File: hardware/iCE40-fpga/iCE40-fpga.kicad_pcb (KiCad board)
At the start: 4 copper layers, 50 x 22.9 mm, 69 parts, among them J1 USB_B_Micro, J2 JST_PH, J3 Feather, Q1 DMP2045U, U1 MCP73831-2-OT, U2 W25Q32JVZP, U3 AP2112K-3.3, U4 ICE40UP5K-SG48ITR, U5 NCV8114ASN120T1G, U6 93C46B, U7 FT2232H, X1 DSC6101CI1A

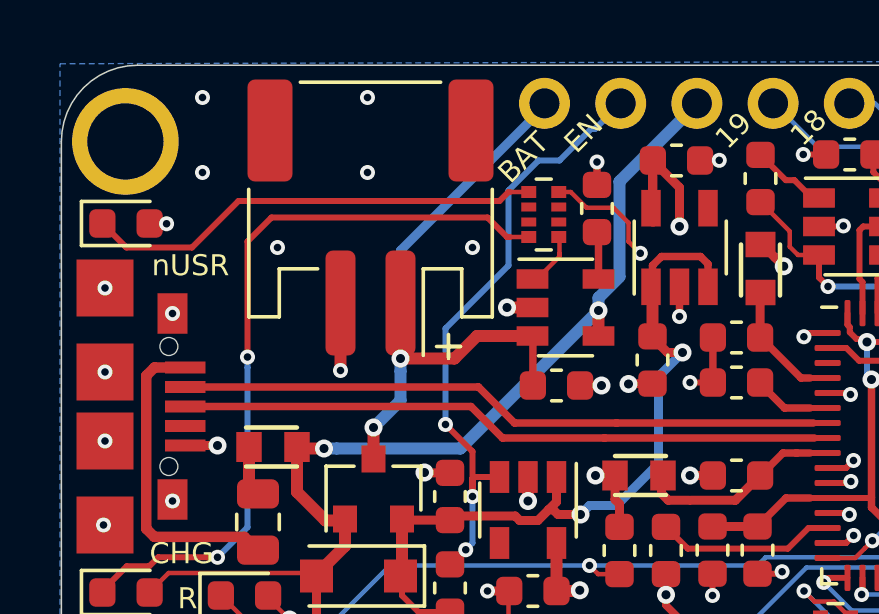
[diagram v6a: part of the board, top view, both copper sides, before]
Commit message: moved battery connector and generated new gerbers for FPGA
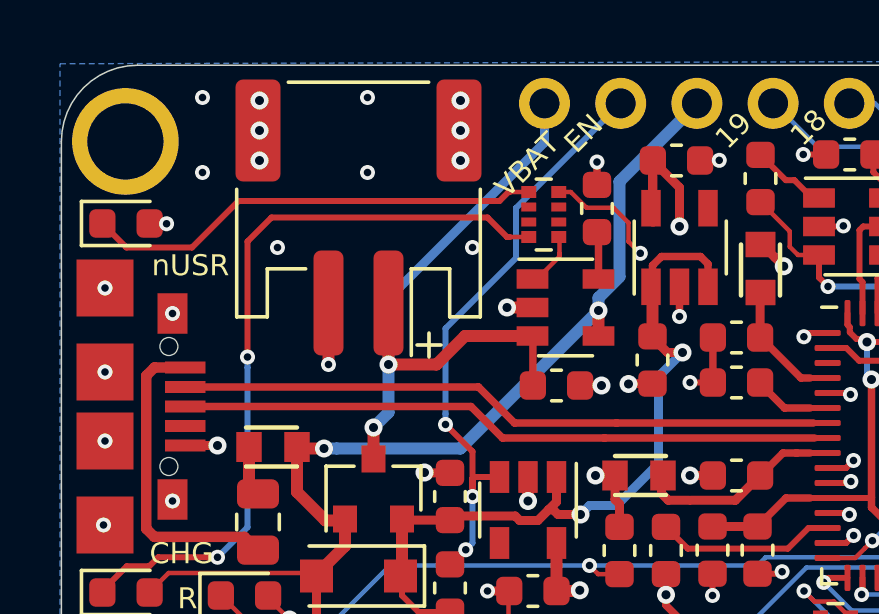
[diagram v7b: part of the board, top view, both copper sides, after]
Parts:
- moved J2 0.40 mm to (36.2, 27.5)
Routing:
- net GND: track 46.5 -> 44.5 mm
- net (no net): vias 0 -> 6
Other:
- board text added: "VBAT"
- board text removed: "BAT"
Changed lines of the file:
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@@
   (general
     (thickness 1.6)
-    (drawings 59)
+    (drawings 58)
     (tracks 1362)
     (zones 0)
@@
   )
   (module josh-connectors:JST_PH_S2B-PH-SM4-TB_1x02-1MP_P2.00mm_Horizontal (layer F.Cu)
-    (at 36.6 27.5 180)
+    (at 36.2 27.5 180)
     (descr "JST PH series connector, S2B-PH-SM4-TB (http://www.jst-mfg.com/product/pdf/eng/ePH.pdf), generated with kicad-footprint-generator")
     (tags "connector JST PH top entry")
@@
       (effects (font (size 1 1) (thickness 0.15)) (justify mirror))
     )
-    (fp_text value 21 (at -2.475 -0.025) (layer B.SilkS)
+    (fp_text value 21 (at -2.4 -0.025) (layer B.SilkS)
       (effects (font (size 1 1) (thickness 0.15)) (justify mirror))
     )
@@
       (effects (font (size 1 1) (thickness 0.15)) (justify mirror))
     )
-    (fp_text value 23 (at -2.5 0) (layer B.SilkS)
+    (fp_text value 23 (at -2.4 0) (layer B.SilkS)
       (effects (font (size 1 1) (thickness 0.15)) (justify mirror))
     )
@@
       (effects (font (size 1 1) (thickness 0.15)) (justify mirror))
     )
-    (fp_text value 20 (at 2.525 0) (layer B.SilkS)
+    (fp_text value 20 (at 2.35 0) (layer B.SilkS)
       (effects (font (size 1 1) (thickness 0.15)) (justify mirror))
     )
@@
       (effects (font (size 1 1) (thickness 0.15)) (justify mirror))
     )
-    (fp_text value 22 (at 2.5 0) (layer B.SilkS)
+    (fp_text value 22 (at 2.35 0) (layer B.SilkS)
       (effects (font (size 1 1) (thickness 0.15)) (justify mirror))
     )
@@
     )
   )
-  (gr_line (start 39.6 31.8) (end 38.8 31.8) (layer F.SilkS) (width 0.12))
-  (gr_line (start 39.2 31.8) (end 39.6 31.8) (layer F.SilkS) (width 0.12))
-  (gr_line (start 39.2 31.4) (end 39.2 32.2) (layer F.SilkS) (width 0.12))
+  (gr_line (start 38.95 31.75) (end 38.15 31.75) (layer F.SilkS) (width 0.12))
+  (gr_line (start 38.55 31.35) (end 38.55 32.15) (layer F.SilkS) (width 0.12))
   (gr_text 14 (at 62.7 25.575) (layer B.SilkS)
     (effects (font (size 1 1) (thickness 0.15)) (justify mirror))
@@
     (effects (font (size 1 1) (thickness 0.15)) (justify mirror))
   )
-  (gr_text BAT (at 42.375 25.575) (layer B.SilkS)
+  (gr_text VBAT (at 41.95 25.6) (layer B.SilkS)
     (effects (font (size 1 1) (thickness 0.15)) (justify mirror))
   )
@@
     (effects (font (size 0.7 0.7) (thickness 0.125)))
   )
-  (gr_text BAT (at 41.7 25.5 45) (layer F.SilkS)
+  (gr_text VBAT (at 41.825 25.75 45) (layer F.SilkS)
     (effects (font (size 0.7 0.7) (thickness 0.125)))
   )
@@
     (effects (font (size 0.7 0.7) (thickness 0.15)))
   )
+  (via (at 32.9 25.6) (size 0.6) (drill 0.3) (layers F.Cu B.Cu) (net 0))
+  (via (at 32.9 24.6) (size 0.6) (drill 0.3) (layers F.Cu B.Cu) (net 0))
+  (via (at 32.9 23.6) (size 0.6) (drill 0.3) (layers F.Cu B.Cu) (net 0))
+  (via (at 39.6 23.6) (size 0.6) (drill 0.3) (layers F.Cu B.Cu) (net 0))
+  (via (at 39.6 25.6) (size 0.6) (drill 0.3) (layers F.Cu B.Cu) (net 0))
+  (via (at 39.6 24.6) (size 0.6) (drill 0.3) (layers F.Cu B.Cu) (net 0))
   (segment (start 39.25 37.5875) (end 37.6875 37.5875) (width 0.3) (layer F.Cu) (net 1))
   (segment (start 37.6875 37.5875) (end 37.65 37.55) (width 0.3) (layer F.Cu) (net 1))
@@
   (segment (start 42.0125 31.4625) (end 42 31.45) (width 0.25) (layer F.Cu) (net 2))
   (segment (start 42.35 23.65) (end 42.4 23.7) (width 0.3) (layer B.Cu) (net 2))
-  (segment (start 37.6 30.35) (end 37.6 29.6) (width 0.4) (layer F.Cu) (net 2))
-  (segment (start 37.6 33.6) (end 37.6 32.624276) (width 0.4) (layer B.Cu) (net 2))
-  (segment (start 37.6 32.624276) (end 37.6 32.200012) (width 0.4) (layer B.Cu) (net 2))
-  (segment (start 37.6 28.6) (end 37.6 31.775748) (width 0.3) (layer B.Cu) (net 2))
-  (via (at 37.6 32.200012) (size 0.6) (drill 0.3) (layers F.Cu B.Cu) (net 2))
-  (segment (start 37.6 31.775748) (end 37.6 32.200012) (width 0.3) (layer B.Cu) (net 2))
-  (segment (start 42.4 23.8) (end 37.6 28.6) (width 0.3) (layer B.Cu) (net 2))
-  (segment (start 36.7 34.5) (end 37.6 33.6) (width 0.4) (layer B.Cu) (net 2))
-  (segment (start 37.6 30.8) (end 37.6 32.200012) (width 0.4) (layer F.Cu) (net 2))
-  (segment (start 37.600012 32.2) (end 37.6 32.200012) (width 0.4) (layer F.Cu) (net 2))
-  (segment (start 39.4 32.2) (end 37.600012 32.2) (width 0.4) (layer F.Cu) (net 2))
-  (segment (start 42 31.45) (end 40.15 31.45) (width 0.4) (layer F.Cu) (net 2))
-  (segment (start 40.15 31.45) (end 39.4 32.2) (width 0.4) (layer F.Cu) (net 2))
+  (segment (start 36.7 34.5) (end 37.2 34) (width 0.4) (layer B.Cu) (net 2))
+  (segment (start 42.4 23.8) (end 42.4 25) (width 0.3) (layer B.Cu) (net 2))
+  (segment (start 42.4 25) (end 37.2 30.2) (width 0.3) (layer B.Cu) (net 2))
+  (segment (start 37.2 31) (end 37.2 30.2) (width 0.4) (layer B.Cu) (net 2))
+  (via (at 37.2 32.4) (size 0.6) (drill 0.3) (layers F.Cu B.Cu) (net 2))
+  (segment (start 37.2 34) (end 37.2 32.4) (width 0.4) (layer B.Cu) (net 2))
+  (segment (start 37.2 32.4) (end 37.2 31) (width 0.4) (layer B.Cu) (net 2))
+  (segment (start 37.2 32.4) (end 37.2 30.5) (width 0.4) (layer F.Cu) (net 2))
+  (segment (start 41.95 31.45) (end 42 31.5) (width 0.4) (layer F.Cu) (net 2))
+  (segment (start 39.75 31.45) (end 41.95 31.45) (width 0.4) (layer F.Cu) (net 2))
+  (segment (start 37.2 32.4) (end 38.8 32.4) (width 0.4) (layer F.Cu) (net 2))
+  (segment (start 38.8 32.4) (end 39.75 31.45) (width 0.4) (layer F.Cu) (net 2))
   (segment (start 56.5 30.6875) (end 56.5 30.15) (width 0.2) (layer F.Cu) (net 3))
   (segment (start 59.5 39.5125) (end 59.5 40.05) (width 0.2) (layer F.Cu) (net 3))
@@
   (segment (start 39.7375 38.575) (end 39.775 38.575) (width 0.2) (layer F.Cu) (net 15))
   (segment (start 45.030001 23.805001) (end 44.95 23.725) (width 0.2) (layer F.Cu) (net 15))
-  (segment (start 44.090001 24.545) (end 43.955 24.545) (width 0.2) (layer B.Cu) (net 15))
-  (segment (start 44.94 23.695001) (end 44.090001 24.545) (width 0.2) (layer B.Cu) (net 15))
-  (segment (start 43.955 24.545) (end 42.9 25.6) (width 0.2) (layer B.Cu) (net 15))
-  (segment (start 42.9 25.6) (end 42.2 25.6) (width 0.2) (layer B.Cu) (net 15))
-  (segment (start 42.2 25.6) (end 41.2 26.6) (width 0.2) (layer B.Cu) (net 15))
-  (segment (start 41.2 26.6) (end 41.2 29.1) (width 0.2) (layer B.Cu) (net 15))
   (via (at 39.1 34.4) (size 0.5) (drill 0.25) (layers F.Cu B.Cu) (net 15))
-  (segment (start 41.2 29.1) (end 39.1 31.2) (width 0.2) (layer B.Cu) (net 15))
-  (segment (start 39.1 31.2) (end 39.1 34.4) (width 0.2) (layer B.Cu) (net 15))
   (segment (start 40.05 36.15) (end 40.9 36.15) (width 0.2) (layer F.Cu) (net 15))
   (segment (start 40 36.8) (end 40 36.2) (width 0.2) (layer F.Cu) (net 15))
@@
   (segment (start 40 35.3) (end 40 36.8) (width 0.2) (layer F.Cu) (net 15))
   (segment (start 39.1 34.4) (end 40 35.3) (width 0.2) (layer F.Cu) (net 15))
+  (segment (start 41.450011 28.849989) (end 39.1 31.2) (width 0.2) (layer B.Cu) (net 15))
+  (segment (start 39.1 31.2) (end 39.1 34.046447) (width 0.2) (layer B.Cu) (net 15))
+  (segment (start 41.450011 27.18499) (end 41.450011 28.849989) (width 0.2) (layer B.Cu) (net 15))
+  (segment (start 44.94 23.695001) (end 41.450011 27.18499) (width 0.2) (layer B.Cu) (net 15))
+  (segment (start 39.1 34.046447) (end 39.1 34.4) (width 0.2) (layer B.Cu) (net 15))
   (via (at 55.925734 38.36152) (size 0.5) (drill 0.25) (layers F.Cu B.Cu) (net 16))
   (via (at 59.65 33.25) (size 0.5) (drill 0.25) (layers F.Cu B.Cu) (net 16))
@@
   (segment (start 49.5875 31.5) (end 49.5875 29.9625) (width 0.3) (layer F.Cu) (net 31))
   (segment (start 49.5875 29.9625) (end 49.6 29.95) (width 0.3) (layer F.Cu) (net 31))
-  (segment (start 35.6 30.35) (end 35.6 31.3) (width 0.4) (layer F.Cu) (net 32))
   (via (at 63.05 29) (size 0.5) (drill 0.25) (layers F.Cu B.Cu) (net 32))
   (via (at 63.075 25.5) (size 0.5) (drill 0.25) (layers F.Cu B.Cu) (net 32))
@@
   (via (at 58.052412 29.099953) (size 0.6) (drill 0.3) (layers F.Cu B.Cu) (net 32))
   (segment (start 58.1 28.4) (end 58.052412 28.447588) (width 0.2) (layer F.Cu) (net 32))
-  (segment (start 35.6 30.35) (end 35.6 31.8) (width 0.4) (layer F.Cu) (net 32))
-  (via (at 35.6 32.6) (size 0.5) (drill 0.25) (layers F.Cu B.Cu) (net 32))
-  (segment (start 35.6 31.8) (end 35.6 32.6) (width 0.4) (layer F.Cu) (net 32))
+  (via (at 35.2 32.4) (size 0.5) (drill 0.25) (layers F.Cu B.Cu) (net 32))
+  (segment (start 35.2 32.4) (end 35.2 31.2) (width 0.4) (layer F.Cu) (net 32))
   (segment (start 51.8375 34.85) (end 51.4 34.85) (width 0.2) (layer F.Cu) (net 33))
   (segment (start 44.4 34.85) (end 51.4 34.85) (width 0.25) (layer F.Cu) (net 33))

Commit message: updated readme
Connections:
- RN2 pad 1: Net-(RN2-Pad1) -> (no net)
- RN3 pad 3: Net-(RN3-Pad3) -> (no net)
- RN3 pad 6: Net-(RN3-Pad6) -> (no net)
- RN4 pad 1: Net-(RN4-Pad1) -> (no net)
- RN5 pad 2: Net-(RN5-Pad2) -> (no net)
- RN5 pad 3: Net-(RN5-Pad3) -> (no net)
- RN5 pad 6: Net-(RN5-Pad6) -> (no net)
- RN5 pad 7: Net-(RN5-Pad7) -> (no net)
- U3 pad 4: Net-(U3-Pad4) -> (no net)
- U5 pad 4: Net-(U5-Pad4) -> (no net)
